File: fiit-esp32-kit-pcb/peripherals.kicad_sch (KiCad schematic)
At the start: 15 parts, among them Q2 SFH320, SW1 SPST NO, SW2 SPST NO, SW3 SPST NO, SW4 SPST NO, U4 AHT20

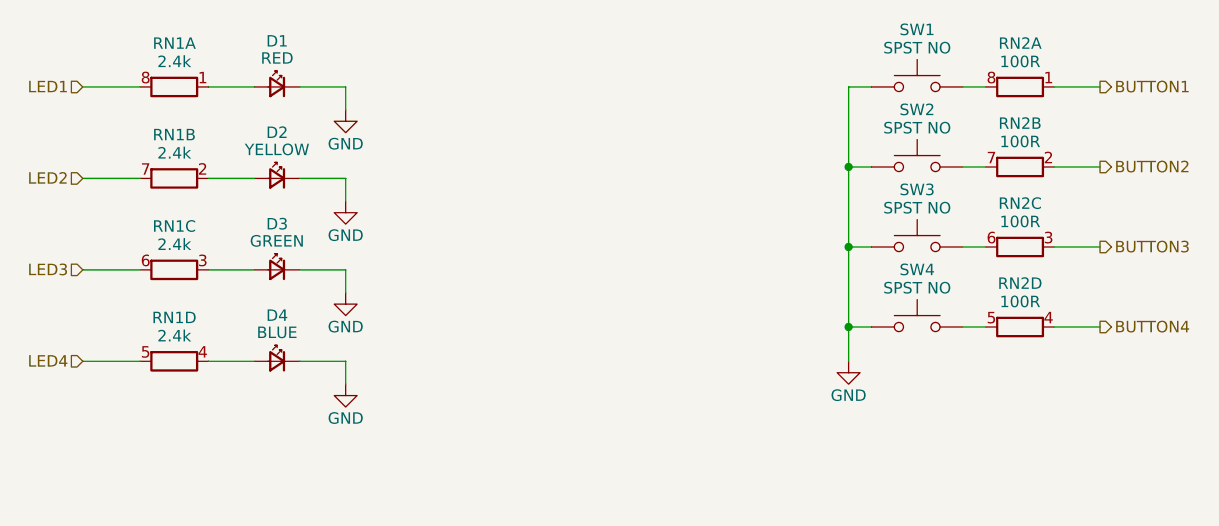
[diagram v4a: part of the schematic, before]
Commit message: added some tracks (unrouted 107)
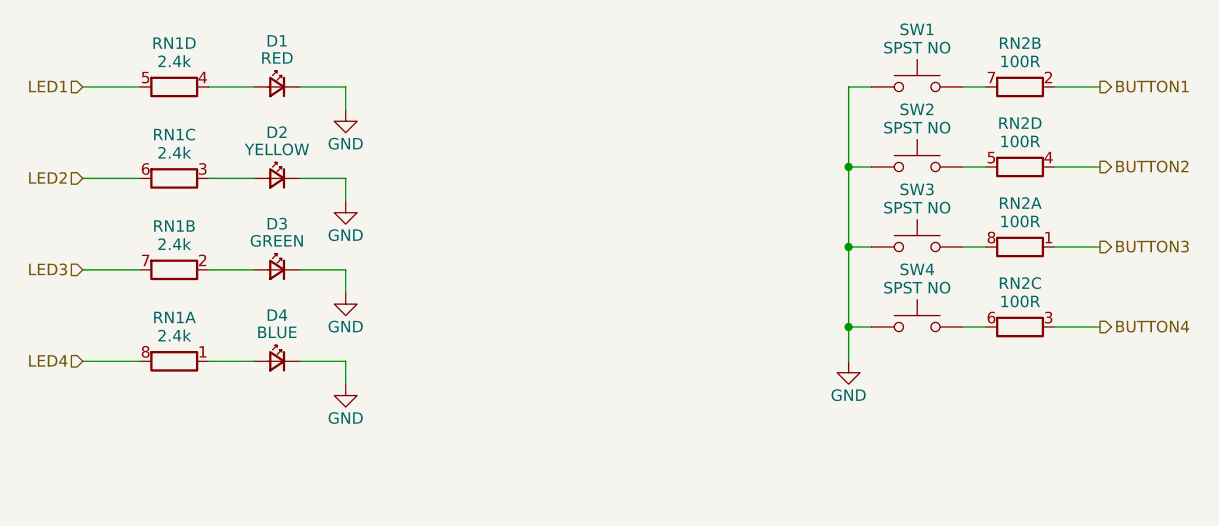
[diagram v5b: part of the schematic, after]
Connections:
- net BUTTON1: now also RN2.2 (R2.1); no longer RN2.1 (R1.1)
- net BUTTON2: now also RN2.4 (R4.1); no longer RN2.2 (R2.1)
- net BUTTON3: now also RN2.1 (R1.1); no longer RN2.3 (R3.1)
- net BUTTON4: now also RN2.3 (R3.1); no longer RN2.4 (R4.1)
- net LED1: now also RN1.5 (R4.2); no longer RN1.8 (R1.2)
- net LED2: now also RN1.6 (R3.2); no longer RN1.7 (R2.2)
- net LED3: now also RN1.7 (R2.2); no longer RN1.6 (R3.2)
- net LED4: now also RN1.8 (R1.2); no longer RN1.5 (R4.2)
- net at D2.2 (A): now also RN1.3 (R3.1); no longer RN1.2 (R2.1)
- net at D3.2 (A): now also RN1.2 (R2.1); no longer RN1.3 (R3.1)
- net at SW3.2: now also RN2.8 (R1.2); no longer RN2.6 (R3.2)
- net at D1.2 (A): now also RN1.4 (R4.1); no longer RN1.1 (R1.1)
- net at SW2.2: now also RN2.5 (R4.2); no longer RN2.7 (R2.2)
- net at SW1.2: now also RN2.7 (R2.2); no longer RN2.8 (R1.2)
- net at D4.2 (A): now also RN1.1 (R1.1); no longer RN1.4 (R4.1)
- net at SW4.2: now also RN2.6 (R3.2); no longer RN2.5 (R4.2)
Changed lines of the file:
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@@
 		(lib_id "Device:R_Pack04_Split")
 		(at 59.69 62.23 90)
-		(unit 2)
+		(unit 3)
 		(exclude_from_sim no)
 		(in_bom yes)
@@
 				(path "/d7013812-ce13-4db9-a6cc-42acdc5acaf9/fe4defb8-cb63-4770-8d91-1c7f8da70e07"
 					(reference "RN1")
-					(unit 2)
+					(unit 3)
 				)
 			)
@@
 		(lib_id "Device:R_Pack04_Split")
 		(at 59.69 72.39 90)
-		(unit 3)
+		(unit 2)
 		(exclude_from_sim no)
 		(in_bom yes)
@@
 				(path "/d7013812-ce13-4db9-a6cc-42acdc5acaf9/fe4defb8-cb63-4770-8d91-1c7f8da70e07"
 					(reference "RN1")
-					(unit 3)
+					(unit 2)
 				)
 			)
@@
 		(lib_id "Device:R_Pack04_Split")
 		(at 153.67 69.85 90)
-		(unit 3)
+		(unit 1)
 		(exclude_from_sim no)
 		(in_bom yes)
@@
 				(path "/d7013812-ce13-4db9-a6cc-42acdc5acaf9/fe4defb8-cb63-4770-8d91-1c7f8da70e07"
 					(reference "RN2")
-					(unit 3)
+					(unit 1)
 				)
 			)
@@
 		(lib_id "Device:R_Pack04_Split")
 		(at 153.67 60.96 90)
-		(unit 2)
+		(unit 4)
 		(exclude_from_sim no)
 		(in_bom yes)
@@
 				(path "/d7013812-ce13-4db9-a6cc-42acdc5acaf9/fe4defb8-cb63-4770-8d91-1c7f8da70e07"
 					(reference "RN2")
-					(unit 2)
+					(unit 4)
 				)
 			)
@@
 		(lib_id "Device:R_Pack04_Split")
 		(at 153.67 52.07 90)
-		(unit 1)
+		(unit 2)
 		(exclude_from_sim no)
 		(in_bom yes)
@@
 				(path "/d7013812-ce13-4db9-a6cc-42acdc5acaf9/fe4defb8-cb63-4770-8d91-1c7f8da70e07"
 					(reference "RN2")
-					(unit 1)
+					(unit 2)
 				)
 			)
@@
 		(lib_id "Device:R_Pack04_Split")
 		(at 59.69 82.55 90)
-		(unit 4)
+		(unit 1)
 		(exclude_from_sim no)
 		(in_bom yes)
@@
 				(path "/d7013812-ce13-4db9-a6cc-42acdc5acaf9/fe4defb8-cb63-4770-8d91-1c7f8da70e07"
 					(reference "RN1")
-					(unit 4)
+					(unit 1)
 				)
 			)
@@
 		(lib_id "Device:R_Pack04_Split")
 		(at 153.67 78.74 90)
-		(unit 4)
+		(unit 3)
 		(exclude_from_sim no)
 		(in_bom yes)
@@
 				(path "/d7013812-ce13-4db9-a6cc-42acdc5acaf9/fe4defb8-cb63-4770-8d91-1c7f8da70e07"
 					(reference "RN2")
-					(unit 4)
+					(unit 3)
 				)
 			)
@@
 		(lib_id "Device:R_Pack04_Split")
 		(at 59.69 52.07 90)
-		(unit 1)
+		(unit 4)
 		(exclude_from_sim no)
 		(in_bom yes)
@@
 				(path "/d7013812-ce13-4db9-a6cc-42acdc5acaf9/fe4defb8-cb63-4770-8d91-1c7f8da70e07"
 					(reference "RN1")
-					(unit 1)
-				)
-			)
+					(unit 4)
+				)
+			)
